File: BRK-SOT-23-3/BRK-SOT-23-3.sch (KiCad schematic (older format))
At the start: 4 parts, among them J1 Conn_01x03, J2 Conn_01x03, U1 Conn_01x03, U2 Conn_01x03

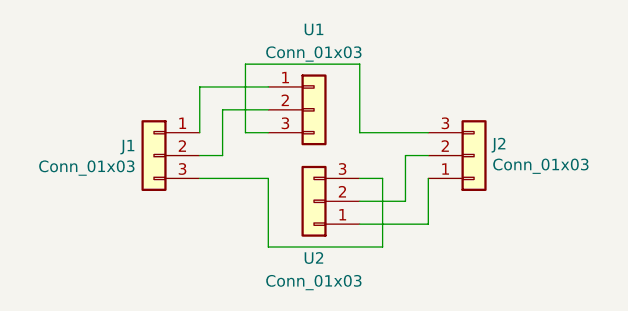
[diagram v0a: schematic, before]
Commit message: BRK-SOT-23-6, BSK-MSOP-8-3x3-P0.65, BRK-VSSOP-8-2.4x2.1-P0.5
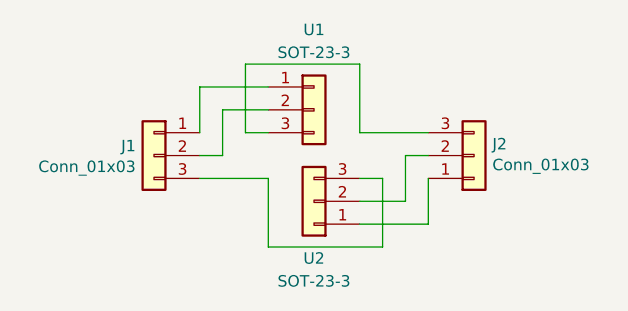
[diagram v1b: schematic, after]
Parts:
- U1, U2: value Conn_01x03 -> SOT-23-3
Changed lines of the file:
@@
 P 6800 3900
 F 0 "U1" H 6800 4250 50  0000 C CNN
-F 1 "Conn_01x03" H 6800 4150 50  0000 C CNN
+F 1 "SOT-23-3" H 6800 4150 50  0000 C CNN
 F 2 "Package_TO_SOT_SMD:SOT-23_Handsoldering" H 6800 3900 50  0001 C CNN
 F 3 "~" H 6800 3900 50  0001 C CNN
@@
 P 6800 4300
 F 0 "U2" H 6800 4550 50  0000 C CNN
-F 1 "Conn_01x03" H 6800 4650 50  0000 C CNN
+F 1 "SOT-23-3" H 6800 4650 50  0000 C CNN
 F 2 "Package_TO_SOT_SMD:SOT-23_Handsoldering" H 6800 4300 50  0001 C CNN
 F 3 "~" H 6800 4300 50  0001 C CNN
